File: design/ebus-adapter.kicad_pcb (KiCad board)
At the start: 2 copper layers, 64.3 x 65.4 mm, 53 parts, among them J1 EBUS, J2 USB_B_Micro, J3 UART, J4 PROG, J5 PINS, J6 PWR, J7 UART, J8 Measurements, Q1 BC817, U1 LM393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

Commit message: Raspberry board update
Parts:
- removed C2, C4: 100nF, Capacitor_SMD:C_1206_3216Metric
- removed C3, C5: 100uF, Capacitor_SMD:CP_Elec_6.3x5.4
- removed H5, H6, H7, H8: MountingHole, MountingHole:MountingHole_3.2mm_M3
- removed J2: USB_B_Micro, usb:AMPHENOL_10118194-0001LF
- removed J4: PROG, Connector_PinHeader_2.54mm:PinHeader_1x06_P2.54mm_Vertical
- removed J5: PINS, Connector_PinHeader_2.54mm:PinHeader_1x06_P2.54mm_Vertical
- removed J6: PWR, Connector_PinHeader_2.54mm:PinHeader_1x02_P2.54mm_Vertical
- removed J7: UART, Connector_PinHeader_2.54mm:PinHeader_2x05_P2.54mm_Vertical
- removed R18: 10k, Resistor_SMD:R_1206_3216Metric
- removed R20, R21: 4.7k, Resistor_SMD:R_1206_3216Metric
- removed U5: AMS1117-3.3, Package_TO_SOT_SMD:SOT-223-3_TabPin2
- removed U6: ESP-12F, RF_Module:ESP-12E
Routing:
- removed copper zone on B.Cu, net GNDREF
- removed copper zone on F.Cu, net GNDREF
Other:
- board size 64.3 x 65.4 mm -> 30.1 x 65.3 mm
- board text removed: "+5V"
- board text removed: "IO0"
- board text removed: "IO12"
- board text removed: "IO13"
- board text removed: "IO14"
- board text removed: "IO16"
- board text removed: "IO4"
- board text removed: "PINS"
- board text removed: "RST"
- board text removed: "RX0"
- board text removed: "SERVICE PORT"
- board text removed: "TX0"
- board text removed: "wifi module"

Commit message: Gerbers
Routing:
- net GNDREF: track 218.0 -> 64.0 mm, vias 3 -> 1
- net +3V3: track 173.7 -> 62.5 mm, vias 4 -> 1
- net RX: track 112.8 -> 60.0 mm, vias 4 -> 1
- net +5VP: track 49.5 -> 0.00 mm, vias 2 -> 0
- net TX: track 65.5 -> 18.4 mm, vias 4 -> 1
- net RESET: track 46.9 -> 0.00 mm
- net P_TX: track 41.0 -> 0.00 mm, vias 2 -> 0
- net GPIO4: track 38.4 -> 0.00 mm
- net P_RX: track 37.1 -> 0.00 mm, vias 2 -> 0
- net GPIO0: track 29.9 -> 0.00 mm, vias 2 -> 0
- net Net-(R18-Pad1): track 23.0 -> 0.00 mm
- net GPIO12: track 10.6 -> 0.00 mm
- net GPIO13: track 5.88 -> 0.00 mm
- net GPIO16: track 5.50 -> 0.00 mm
- net GPIO14: track 5.37 -> 0.00 mm
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
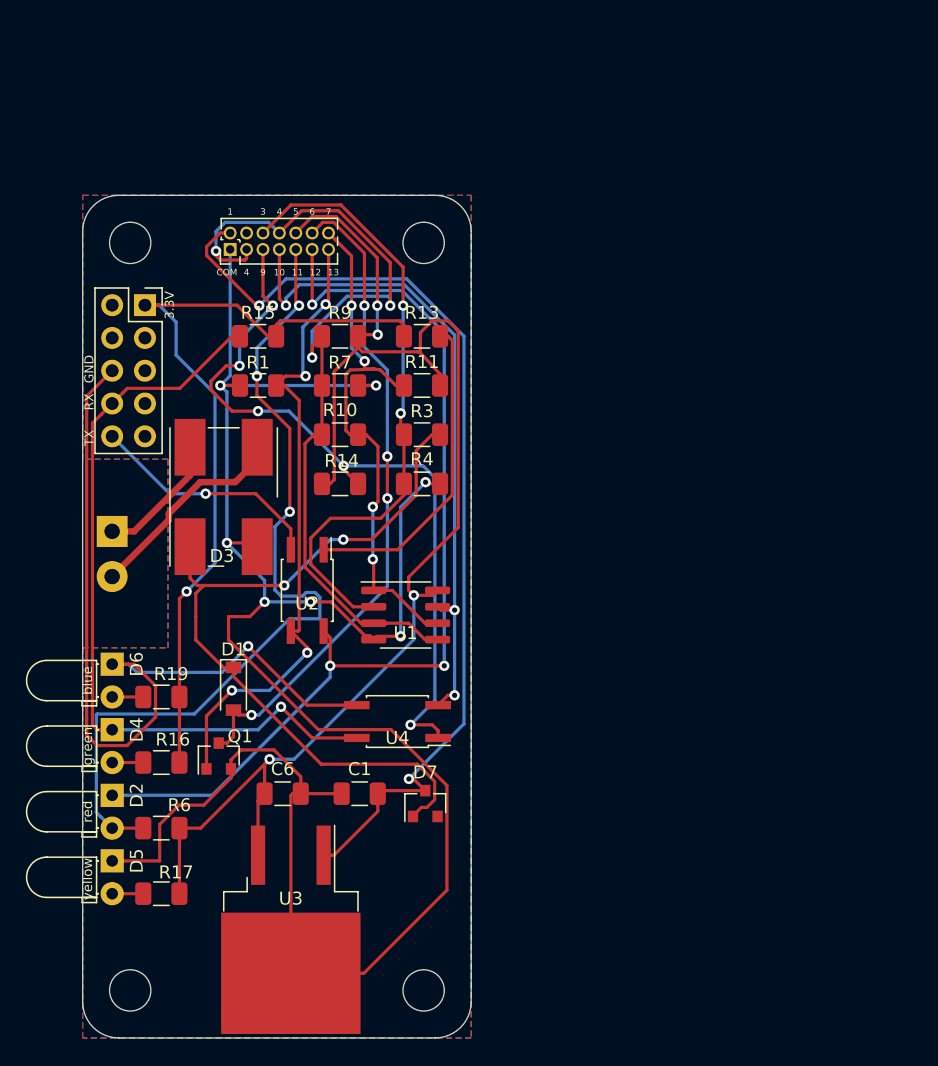
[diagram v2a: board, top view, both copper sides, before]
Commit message: Inverted rx-tx, reposition ebus terminal with measurement points to let attach raspberry with full connector, added programmer to wifi module
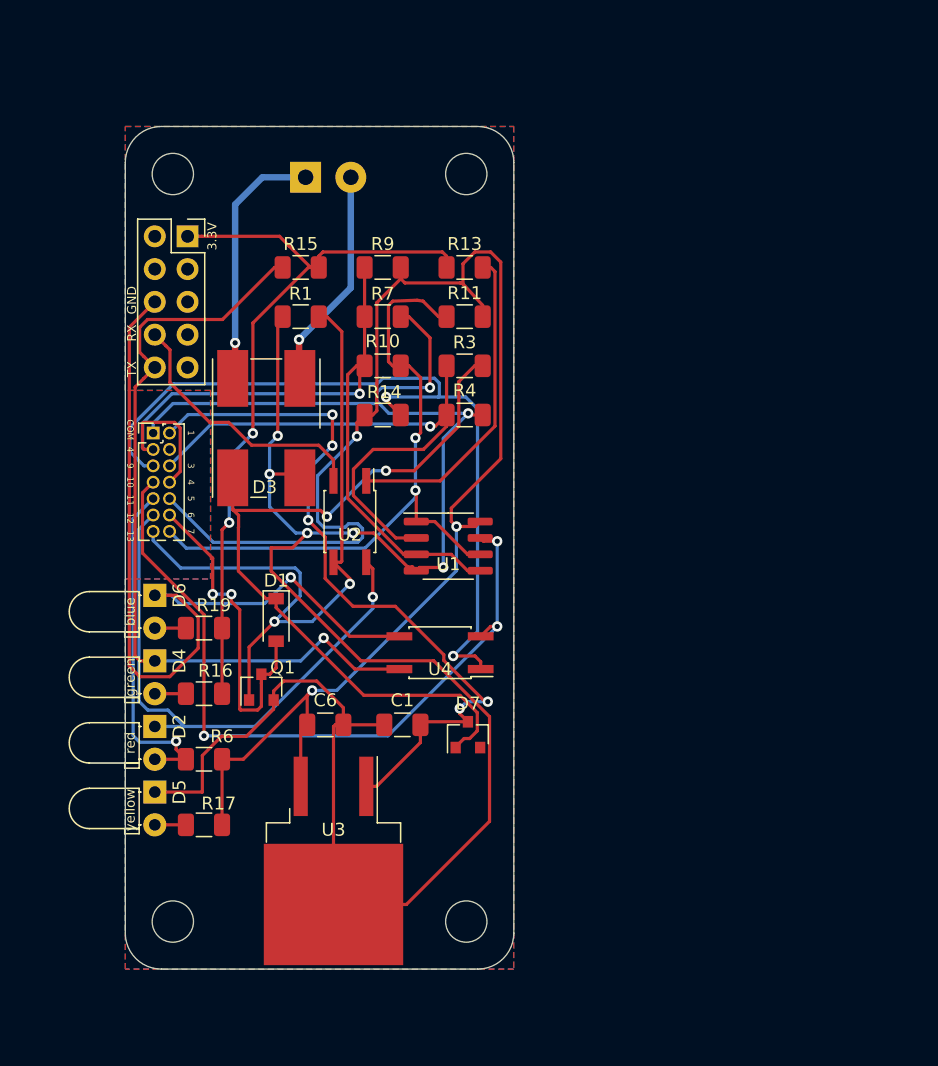
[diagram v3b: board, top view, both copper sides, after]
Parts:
- J8: value Measurements -> Conn_02x07_Counter_Clockwise
- moved J1 31.3 mm to (80.5, 81.7), turned to 0 degrees
- moved J8 15.4 mm to (68.7, 101.5), turned to 0 degrees
- moved C6 6.27 mm to (82.0, 124.1)
- moved R6 6.27 mm to (72.6, 126.7)
- moved C1 6.27 mm to (88.0, 124.1)
- moved D7 6.27 mm to (93.1, 124.8)
- moved D5 6.27 mm to (68.8, 129.3)
- moved R1 6.27 mm to (80.1, 92.5)
- moved R11 6.27 mm to (92.8, 92.5)
- moved R13 6.27 mm to (92.8, 88.6)
- moved R15 6.27 mm to (80.1, 88.6)
- moved R16 6.27 mm to (72.6, 121.7)
- moved R17 6.27 mm to (72.6, 131.8)
- moved R19 6.27 mm to (72.6, 116.6)
- moved R4 6.27 mm to (92.8, 100.1)
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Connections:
- C1 pad 1: MP1 -> (no net)
- C1 pad 2: GNDD -> (no net)
- C6 pad 1: MP5 -> (no net)
- C6 pad 2: GNDD -> (no net)
- D1 pad 1: SIGNAL -> (no net)
- D1 pad 2: MP6 -> (no net)
- D2 pad 1: MP12 -> (no net)
- D2 pad 2: MP11 -> (no net)
- D3 pad 1: GNDD -> (no net)
- D3 pad 2: +24V -> (no net)
- D3 pad 3: Net-(D3-Pad3) -> (no net)
- D3 pad 4: SIGNAL -> (no net)
- D4 pad 1: RX -> (no net)
- D4 pad 2: Net-(D4-Pad2) -> (no net)
- D5 pad 1: GNDD -> (no net)
- D5 pad 2: Net-(D5-Pad2) -> (no net)
- D6 pad 1: GNDREF -> (no net)
- D6 pad 2: Net-(D6-Pad2) -> (no net)
- D7 pad 1: SIGNAL -> (no net)
- D7 pad 3: MP1 -> (no net)
- J1 pad 1: Net-(D3-Pad3) -> (no net)
- J1 pad 2: +24V -> (no net)
- J3 pad 1: +3V3 -> (no net)
- J3 pad 10: TX -> (no net)
- J3 pad 6: GNDREF -> (no net)
- J3 pad 8: RX -> (no net)
- J8 pad 1: GNDD -> (no net)
- J8 pad 10: MP5 -> (no net)
- J8 pad 11: MP12 -> (no net)
- J8 pad 12: MP6 -> (no net)
- J8 pad 13: MP13 -> (no net)
- J8 pad 14: MP7 -> (no net)
- J8 pad 2: MP1 -> (no net)
- J8 pad 3: MP4 -> (no net)
- J8 pad 5: MP9 -> (no net)
- J8 pad 6: MP3 -> (no net)
- J8 pad 7: MP10 -> (no net)
- J8 pad 8: MP4 -> (no net)
- J8 pad 9: MP11 -> (no net)
- Q1 pad 1: MP13 -> (no net)
- Q1 pad 2: GNDD -> (no net)
- Q1 pad 3: MP6 -> (no net)
- R1 pad 1: MP13 -> (no net)
- R1 pad 2: GNDD -> (no net)
- R10 pad 1: MP7 -> (no net)
- R10 pad 2: MP4 -> (no net)
- R11 pad 1: MP7 -> (no net)
- R11 pad 2: MP5 -> (no net)
- R13 pad 1: +3V3 -> (no net)
- R13 pad 2: Net-(R13-Pad2) -> (no net)
- R14 pad 1: MP9 -> (no net)
- R14 pad 2: MP5 -> (no net)
- R15 pad 1: RX -> (no net)
- R15 pad 2: +3V3 -> (no net)
- R16 pad 1: Net-(D4-Pad2) -> (no net)
- R16 pad 2: +3V3 -> (no net)
- R17 pad 1: Net-(D5-Pad2) -> (no net)
- R17 pad 2: MP5 -> (no net)
- R19 pad 1: Net-(D6-Pad2) -> (no net)
- R19 pad 2: +3V3 -> (no net)
- R3 pad 1: MP3 -> (no net)
- R3 pad 2: SIGNAL -> (no net)
- R4 pad 1: GNDD -> (no net)
- R4 pad 2: MP3 -> (no net)
- R6 pad 1: MP11 -> (no net)
- R6 pad 2: MP5 -> (no net)
- R7 pad 1: MP4 -> (no net)
- R7 pad 2: GNDD -> (no net)
- R9 pad 1: MP4 -> (no net)
- R9 pad 2: MP5 -> (no net)
- U1 pad 1: MP7 -> (no net)
- U1 pad 2: MP3 -> (no net)
- U1 pad 3: MP4 -> (no net)
- U1 pad 4: GNDD -> (no net)
- U1 pad 5: MP4 -> (no net)
- U1 pad 6: MP7 -> (no net)
- U1 pad 7: MP10 -> (no net)
- U1 pad 8: MP5 -> (no net)
- U2 pad 1: Net-(R13-Pad2) -> (no net)
- U2 pad 2: TX -> (no net)
- U2 pad 3: MP13 -> (no net)
- U2 pad 4: MP12 -> (no net)
- U3 pad 1: MP1 -> (no net)
- U3 pad 2: GNDD -> (no net)
- U3 pad 3: MP5 -> (no net)
- U4 pad 1: MP9 -> (no net)
- U4 pad 2: MP10 -> (no net)
- U4 pad 3: GNDREF -> (no net)
- U4 pad 4: RX -> (no net)
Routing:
- net (no net): track 0.00 -> 1125.0 mm, vias 0 -> 38
- net GNDD: track 162.4 -> 0.00 mm, vias 7 -> 0
- net MP5: track 106.7 -> 0.00 mm, vias 4 -> 0
- net MP1: track 75.9 -> 0.00 mm, vias 2 -> 0
- net MP12: track 75.4 -> 0.00 mm, vias 3 -> 0
- net MP4: track 68.2 -> 0.00 mm, vias 3 -> 0
- net MP11: track 67.1 -> 0.00 mm, vias 3 -> 0
- net GNDREF: track 64.0 -> 0.00 mm, vias 1 -> 0
- net +3V3: track 62.5 -> 0.00 mm, vias 1 -> 0
- net SIGNAL: track 60.5 -> 0.00 mm, vias 2 -> 0
- net RX: track 60.0 -> 0.00 mm, vias 1 -> 0
- net MP9: track 59.0 -> 0.00 mm, vias 5 -> 0
- net MP6: track 51.6 -> 0.00 mm, vias 4 -> 0
- net MP10: track 51.2 -> 0.00 mm, vias 3 -> 0
- net MP13: track 50.2 -> 0.00 mm, vias 4 -> 0
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- added copper zone on F.Cu, net (none)
- removed copper zone on F.Cu, net GNDD

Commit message: usbc, updated images
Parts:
- D2, D4, D5, D6: footprint LED_THT:LED_D3.0mm_Horizontal_O1.27mm_Z2.0mm -> Diode_SMD:D_1206_3216Metric
- R17: value 10k -> 5.1k
- R19: value 10k -> 20k
- moved J1 11.3 mm to (72.3, 73.9)
- moved D3 8.22 mm to (74.8, 93.3)
- moved J3 8.22 mm to (68.7, 78.5)
- moved Q1 8.22 mm to (74.4, 113.4)
- moved R1 8.22 mm to (77.5, 84.7)
- moved R10 8.22 mm to (83.8, 88.5)
- moved R11 8.22 mm to (90.2, 84.7)
- moved R13 8.22 mm to (90.2, 80.9)
- moved R15 8.22 mm to (77.5, 80.9)
- moved R19 8.22 mm to (70.0, 108.8)
- moved R3 8.22 mm to (90.2, 88.5)
- moved R7 8.22 mm to (83.8, 84.7)
- moved R9 8.22 mm to (83.8, 80.9)
- moved U2 8.22 mm to (81.3, 100.6)
- moved U3 8.22 mm to (80.0, 126.8)
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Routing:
- net (no net): track 1125.0 -> 1120.0 mm, vias 38 -> 41
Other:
- net class Default removed
- net class Power removed
- board text removed: "1"
- board text removed: "10"
- board text removed: "11"
- board text removed: "12"
- board text removed: "13"
- board text removed: "3"
- board text removed: "3.3V"
- board text removed: "4"
- board text removed: "5"
- board text removed: "6"
- board text removed: "7"
- board text removed: "9"
- board text removed: "COM"
- board text removed: "GND"
- board text removed: "RX"
- board text removed: "TX"
- board text removed: "blue"
- board text removed: "green"
- board text removed: "red"
- board text removed: "yellow"
- board text removed: "~"
